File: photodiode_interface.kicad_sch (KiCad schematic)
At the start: 41 parts, among them J4 Conn_01x12_Pin, J5 Conn_01x12_Pin, J6 Conn_01x12_Pin, J7 Conn_01x12_Pin, U5 OPA350, U6 SN74LVC16244ADGGR, U7 SN74LVC32A

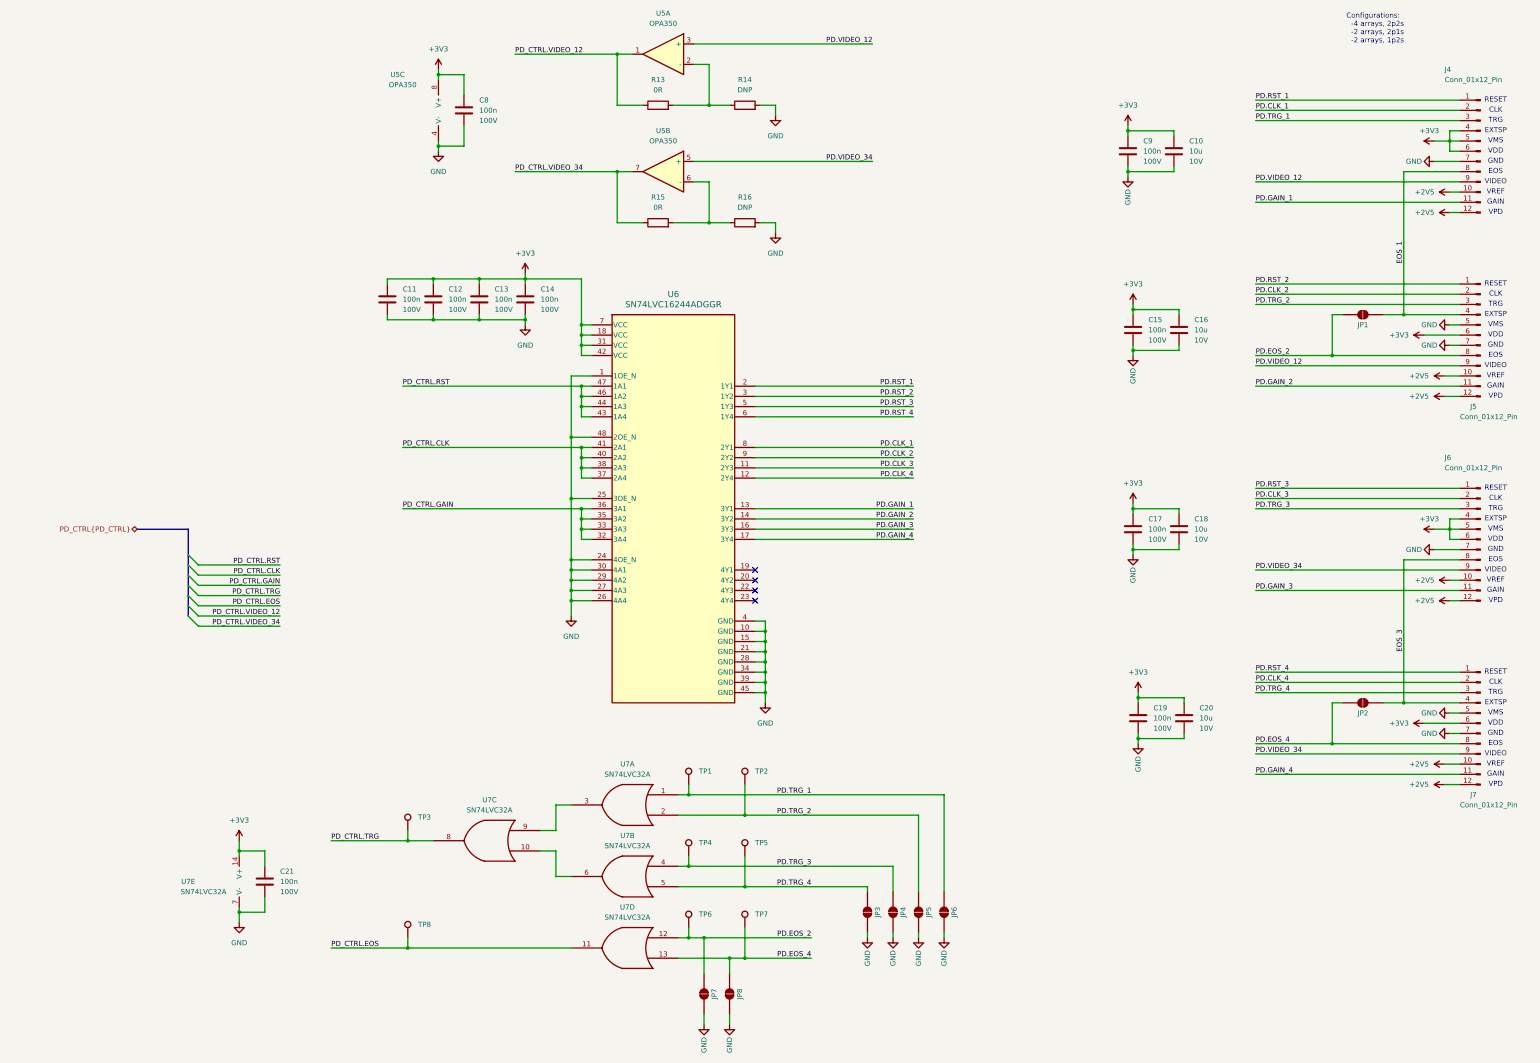
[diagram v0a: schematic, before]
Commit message: nodified according to review
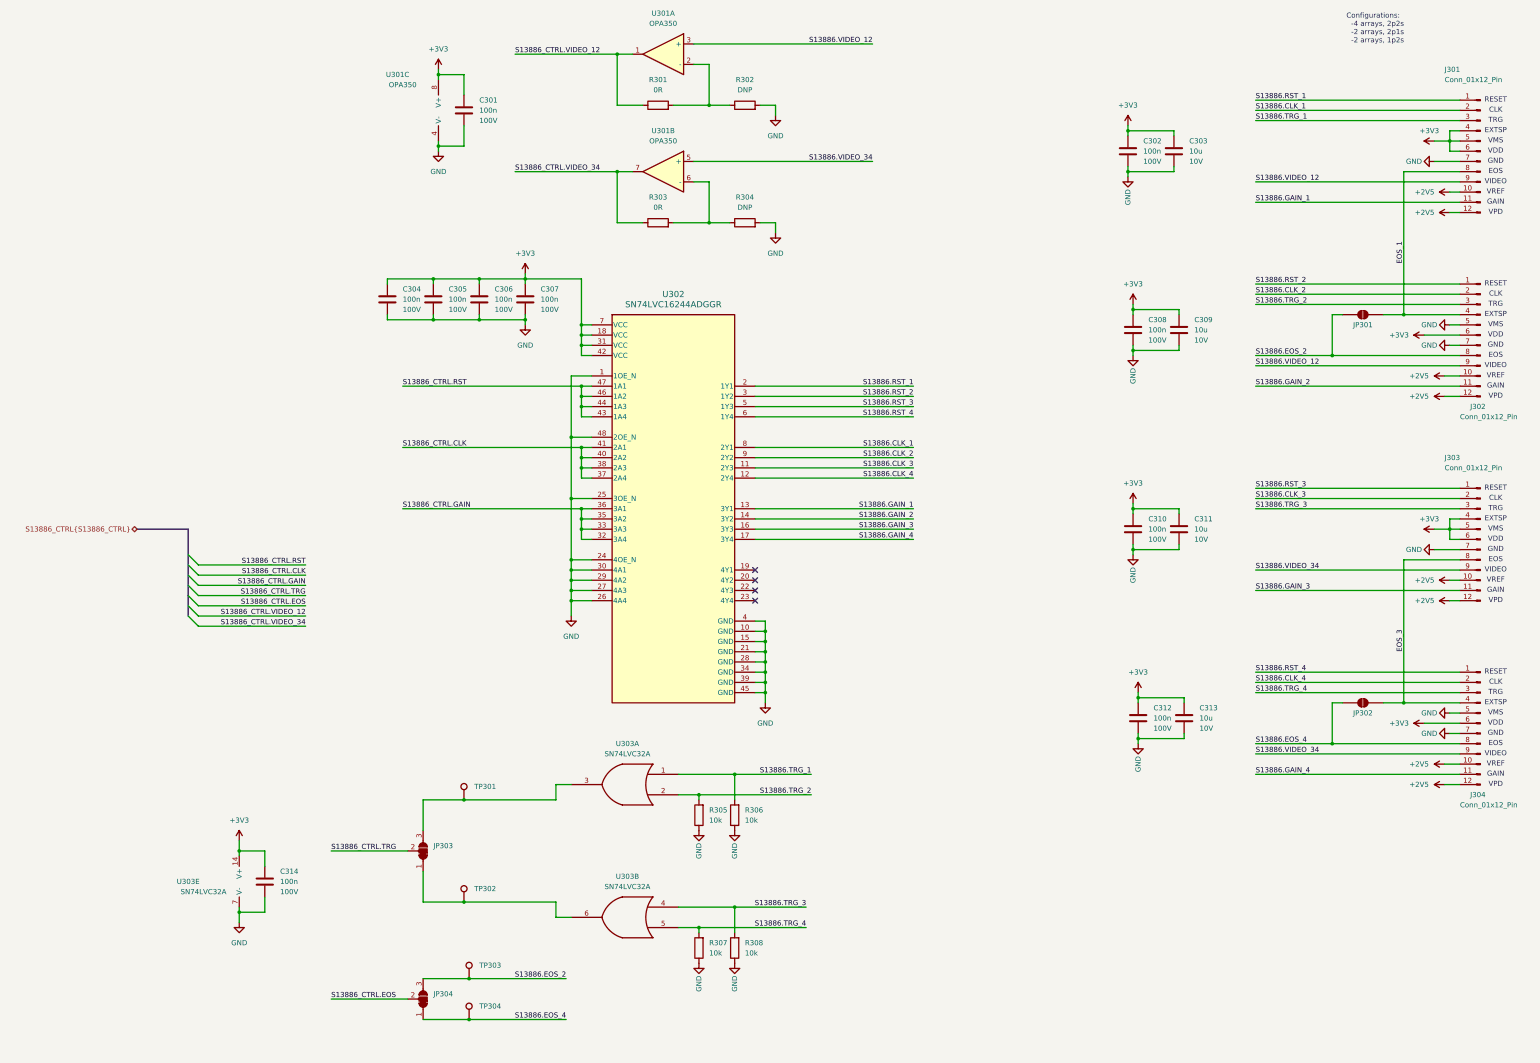
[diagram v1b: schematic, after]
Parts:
- removed JP3, JP4, JP5, JP6, JP7, JP8: SolderJumper_2_Open, symbol Jumper:SolderJumper_2_Open
- removed TP1, TP2, TP3, TP4, TP5, TP8: TestPoint, symbol Connector:TestPoint
- removed unit 4 of U7
- removed unit 3 of U7
- added JP303, JP304: SolderJumper_3_Bridged12, symbol Jumper:SolderJumper_3_Bridged12
- added R305, R306, R307, R308: 10k, symbol Device:R
- added TP301, TP302: TestPoint, symbol Connector:TestPoint
- renumbered C8 to C301, C9 to C302, C10 to C303, C11 to C304, C12 to C305, C13 to C306, C14 to C307, C15 to C308, C16 to C309, C17 to C310, C18 to C311, C19 to C312, C20 to C313, C21 to C314, J4 to J301, J5 to J302, J6 to J303, J7 to J304, JP1 to JP301, JP2 to JP302, R13 to R301, R14 to R302, R15 to R303, R16 to R304, TP6 to TP303, TP7 to TP304, U5 to U301, U6 to U302, U7 to U303
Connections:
- net GND: now also R305.1, R306.1, R307.1, R308.1
- net at U303.3: now also JP303.3 (B), TP301.1
- net at U303.6: now also JP303.1 (A), TP302.1
- net PD.CLK_1 renamed S13886.CLK_1
- net PD.CLK_2 renamed S13886.CLK_2
- net PD.CLK_3 renamed S13886.CLK_3
- net PD.CLK_4 renamed S13886.CLK_4
- net PD.EOS_2 renamed S13886.EOS_2
- net S13886.EOS_2: now also JP304.3 (B)
- net PD.EOS_4 renamed S13886.EOS_4
- net S13886.EOS_4: now also JP304.1 (A)
- net PD.GAIN_1 renamed S13886.GAIN_1
- net PD.GAIN_2 renamed S13886.GAIN_2
- net PD.GAIN_3 renamed S13886.GAIN_3
- net PD.GAIN_4 renamed S13886.GAIN_4
- net PD.RST_1 renamed S13886.RST_1
- net PD.RST_2 renamed S13886.RST_2
- net PD.RST_3 renamed S13886.RST_3
- net PD.RST_4 renamed S13886.RST_4
- net PD.TRG_1 renamed S13886.TRG_1
- net S13886.TRG_1: now also R306.2
- net PD.TRG_2 renamed S13886.TRG_2
- net S13886.TRG_2: now also R305.2
- net PD.TRG_3 renamed S13886.TRG_3
- net S13886.TRG_3: now also R308.2
- net PD.TRG_4 renamed S13886.TRG_4
- net S13886.TRG_4: now also R307.2
- net PD.VIDEO_12 renamed S13886.VIDEO_12
- net PD.VIDEO_34 renamed S13886.VIDEO_34
- net PD_CTRL.CLK renamed S13886_CTRL.CLK
- net PD_CTRL.GAIN renamed S13886_CTRL.GAIN
- net PD_CTRL.RST renamed S13886_CTRL.RST
- net PD_CTRL.VIDEO_12 renamed S13886_CTRL.VIDEO_12
- net PD_CTRL.VIDEO_34 renamed S13886_CTRL.VIDEO_34
- new net S13886_CTRL.EOS: JP304.2 (C)
- new net S13886_CTRL.TRG: JP303.2 (C)
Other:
- company: (none) -> Protonica
- title: (none) -> Front End Electronics
- moved on the sheet: TP303, TP304, U303A, U303B

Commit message: minor changes
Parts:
- removed JP303, JP304: SolderJumper_3_Bridged12, symbol Jumper:SolderJumper_3_Bridged12
- added JP303, JP305: SolderJumper_3_Open, symbol Jumper:SolderJumper_3_Open
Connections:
- net S13886.EOS_2: now also JP303.3 (B)
- net S13886.EOS_4: now also JP303.1 (A)
- net S13886_CTRL.EOS: now also JP303.2 (C)
- net S13886_CTRL.TRG: now also JP305.2 (C)
- net at TP301.1, U303.3: now also JP305.3 (B)
- net at TP302.1, U303.6: now also JP305.1 (A)
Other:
- note added: "Configurations: -4 arrays, 2p2s => JP301 OFF, JP302 OFF -2 arrays, 2p1s => PD1 and PD3, JP301 ON, JP302 ON -2 arrays, 1p2s => PD1 and PD2, JP301 OFF, JP302 OFF"
- note removed: "Configurations: -4 arrays, 2p2s -2 arrays, 2p1s -2 arrays, 1p2s"

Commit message: footprints associated to symbols
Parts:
- C301, C302, C304, C305, C306, C307, C308, C310, C312, C314: footprint (none) -> Capacitor_SMD:C_0805_2012Metric_Pad1.18x1.45mm_HandSolder; MPN (none) -> GCM21BR72A104KA37L; Manufacturer (none) -> Murata Electronics
- C303, C309, C311, C313: footprint (none) -> Capacitor_SMD:C_1206_3216Metric_Pad1.33x1.80mm_HandSolder; MPN (none) -> GRM31CR71E106KA12L; Manufacturer (none) -> Murata Electronics; Voltage 10V -> 25V
- J301, J302, J303, J304: footprint (none) -> Connector_PinHeader_2.54mm:PinHeader_1x12_P2.54mm_Vertical
- JP301, JP302: footprint (none) -> Jumper:SolderJumper-2_P1.3mm_Open_Pad1.0x1.5mm
- JP303, JP305: footprint (none) -> Jumper:SolderJumper-3_P1.3mm_Open_Pad1.0x1.5mm
- R301, R303: footprint (none) -> Resistor_SMD:R_0805_2012Metric_Pad1.20x1.40mm_HandSolder; MPN (none) -> CRCW08050000Z0EA; Manufacturer (none) -> Vishay Dale
- R302, R304: footprint (none) -> Resistor_SMD:R_0805_2012Metric_Pad1.20x1.40mm_HandSolder
- R305, R306, R307, R308: footprint (none) -> Resistor_SMD:R_0805_2012Metric_Pad1.20x1.40mm_HandSolder; MPN (none) -> CRCW080510K0FKEA; Manufacturer (none) -> Vishay Dale
- TP301, TP302, TP303, TP304: footprint (none) -> TestPoint:TestPoint_Keystone_5005-5009_Compact; MPN (none) -> 5005; Manufacturer (none) -> Keystone Electronics
- U301: footprint (none) -> Package_SO:SOIC-8_3.9x4.9mm_P1.27mm; MPN (none) -> OPA350UA/2K5; Manufacturer (none) -> Texas Instruments
- U302: footprint (none) -> Package_SO:TSSOP-48_6.1x12.5mm_P0.5mm; MPN (none) -> SN74LVC16244ADGGR; Manufacturer (none) -> Texas Instrument
- U303: footprint (none) -> Package_SO:SOIC-14_3.9x8.7mm_P1.27mm; MPN (none) -> SN74LVC32ADR; Manufacturer (none) -> Texas Instrument

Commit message: Most tracks routed
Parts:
- removed U303: SN74LVC32A, Package_SO:SOIC-14_3.9x8.7mm_P1.27mm, symbol Logic_Gates_Protonica:SN74LVC32A
- added U303: 74LVC2G32, Package_SO:VSSOP-8_3x3mm_P0.65mm, symbol 74xGxx:74LVC2G32
- J301, J302, J303, J304: footprint Connector_PinHeader_2.54mm:PinHeader_1x12_P2.54mm_Vertical -> Connector_PinHeader_2.54mm:PinHeader_2x06_P2.54mm_Vertical
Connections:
- net +3V3: now also U303.8 (VCC)
- net GND: now also U303.4 (GND)
- net S13886.TRG_1: now also U303.1
- net S13886.TRG_2: now also U303.2
- net S13886.TRG_3: now also U303.5
- net S13886.TRG_4: now also U303.6
- net at JP305.3 (B), TP301.1: now also U303.7
- net at JP305.1 (A), TP302.1: now also U303.3

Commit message: DRC clean
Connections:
- net TRG_12: now reaches JP305.3 (B), TP301.1, U303.7
- net TRG_34: now reaches JP305.1 (A), TP302.1, U303.3
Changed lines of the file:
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@@
+		)
+	)
+	(label "TRG_34"
+		(at 139.7 243.84 0)
+		(effects
+			(font
+				(size 1.27 1.27)
+			)
+			(justify left bottom)
 		)
 	)
@@
 		(effects
 			(font
+				(size 1.27 1.27)
+			)
+			(justify left bottom)
+		)
+	)
+	(label "TRG_12"
+		(at 139.7 218.44 0)
+		(effects
+			(font

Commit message: added stitching vias and silkscreen
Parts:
- added FB301: 220R@100MHz, Inductor_SMD:L_0805_2012Metric_Pad1.05x1.20mm_HandSolder, symbol Device:FerriteBead
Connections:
- net +3V3: now also FB301.1; no longer C301.1, U301.8 (V+)
- new net: C301.1, FB301.2, U301.8 (V+)
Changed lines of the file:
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@@
 	(title_block
 		(title "Front End Electronics")
-		(date "2026-05-05")
+		(date "2026-06-11")
 		(rev "B.1")
 		(company "Protonica")
@@
 	)
 	(junction
+		(at 120.65 38.1)
+		(diameter 0)
+		(color 0 0 0 0)
+	)
+	(junction
 		(at 292.1 52.07)
 		(diameter 0)
@@
 	)
 	(junction
-		(at 120.65 38.1)
-		(diameter 0)
-		(color 0 0 0 0)
-	)
-	(junction
 		(at 119.38 99.06)
 		(diameter 0)
@@
 	(wire
 		(pts
+			(xy 101.6 38.1) (xy 109.22 38.1)
+		)
+		(stroke
+			(width 0)
+			(type default)
+		)
+	)
+	(wire
+		(pts
 			(xy 201.93 184.15) (xy 201.93 186.69)
 		)
@@
 	(wire
 		(pts
-			(xy 120.65 36.83) (xy 120.65 38.1)
+			(xy 130.81 88.9) (xy 130.81 90.17)
 		)
 		(stroke
@@
 	(wire
 		(pts
-			(xy 130.81 88.9) (xy 130.81 90.17)
+			(xy 368.3 156.21) (xy 374.65 156.21)
 		)
 		(stroke
@@
 	(wire
 		(pts
-			(xy 368.3 156.21) (xy 374.65 156.21)
+			(xy 323.85 64.77) (xy 374.65 64.77)
 		)
 		(stroke
@@
 	(wire
 		(pts
-			(xy 323.85 64.77) (xy 374.65 64.77)
+			(xy 199.39 179.07) (xy 201.93 179.07)
 		)
 		(stroke
@@
 	(wire
 		(pts
-			(xy 199.39 179.07) (xy 201.93 179.07)
+			(xy 153.67 128.27) (xy 153.67 113.03)
 		)
 		(stroke
@@
 	(wire
 		(pts
-			(xy 153.67 128.27) (xy 153.67 113.03)
+			(xy 116.84 38.1) (xy 120.65 38.1)
 		)
 		(stroke
@@
 	(wire
 		(pts
+			(xy 101.6 36.83) (xy 101.6 38.1)
+		)
+		(stroke
+			(width 0)
+			(type default)
+		)
+	)
+	(wire
+		(pts
 			(xy 323.85 107.95) (xy 342.9 107.95)
 		)
@@
 	(symbol
 		(lib_id "power:+2V5")
-		(at 120.65 36.83 0)
+		(at 101.6 36.83 0)
 		(unit 1)
 		(body_style 1)
@@
 		(fields_autoplaced yes)
 		(property "Reference" "#PWR0301"
-			(at 120.65 40.64 0)
+			(at 101.6 40.64 0)
 			(hide yes)
 			(show_name no)
@@
 		)
 		(property "Value" "+3V3"
-			(at 120.65 31.75 0)
+			(at 101.6 31.75 0)
 			(show_name no)
 			(do_not_autoplace no)
@@
 		)
 		(property "Footprint" ""
-			(at 120.65 36.83 0)
+			(at 101.6 36.83 0)
 			(hide yes)
 			(show_name no)
@@
 		)
 		(property "Datasheet" ""
-			(at 120.65 36.83 0)
+			(at 101.6 36.83 0)
 			(hide yes)
 			(show_name no)
@@
 		)
 		(property "Description" "Power symbol creates a global label with name \"+2V5\""
-			(at 120.65 36.83 0)
+			(at 101.6 36.83 0)
 			(hide yes)
 			(show_name no)
@@
 	)
 	(symbol
+		(lib_id "Device:FerriteBead")
+		(at 113.03 38.1 90)
+		(unit 1)
+		(body_style 1)
+		(exclude_from_sim no)
+		(in_bom yes)
+		(on_board yes)
+		(in_pos_files yes)
+		(dnp no)
+		(fields_autoplaced yes)
+		(property "Reference" "FB301"
+			(at 112.9792 30.48 90)
+			(show_name no)
+			(do_not_autoplace no)
+			(effects
+				(font
+					(size 1.27 1.27)
+				)
+			)
+		)
+		(property "Value" "220R@100MHz"
+			(at 112.9792 33.02 90)
+			(show_name no)
+			(do_not_autoplace no)
+			(effects
+				(font
+					(size 1.27 1.27)
+				)
+			)
+		)
+		(property "Footprint" "Inductor_SMD:L_0805_2012Metric_Pad1.05x1.20mm_HandSolder"
+			(at 113.03 39.878 90)
+			(hide yes)
+			(show_name no)
+			(do_not_autoplace no)
+			(effects
+				(font
+					(size 1.27 1.27)
+				)
+			)
+		)
+		(property "Datasheet" ""
+			(at 113.03 38.1 0)
+			(hide yes)
+			(show_name no)
+			(do_not_autoplace no)
+			(effects
+				(font
+					(size 1.27 1.27)
+				)
+			)
+		)
+		(property "Description" "FERRITE BEAD 220 OHM 0805 1LN"
+			(at 113.03 38.1 0)
+			(hide yes)
+			(show_name no)
+			(do_not_autoplace no)
+			(effects
+				(font
+					(size 1.27 1.27)
+				)
+			)
+		)
+		(property "MPN" "BLM21PG221SN1D"
+			(at 113.03 38.1 90)
+			(hide yes)
+			(show_name no)
+			(do_not_autoplace no)
+			(effects
+				(font
+					(size 1.27 1.27)
+				)
+			)
+		)
+		(property "Manufacturer" "Murata Electronics"
+			(at 113.03 38.1 90)
+			(hide yes)
+			(show_name no)
+			(do_not_autoplace no)
+			(effects
+				(font
+					(size 1.27 1.27)
+				)
+			)
+		)
+		(property "L (µH)" ""
+			(at 113.03 38.1 90)
+			(hide yes)
+			(show_name no)
+			(do_not_autoplace no)
+			(effects
+				(font
+					(size 1.27 1.27)
+				)
+			)
+		)
+		(pin "1"
+		)
+		(pin "2"
+		)
+		(instances
+			(project "hw-front-end"
+				(path "/87f042ce-f629-4310-aed7-dea93cc7b6f7/4abb1a1f-8324-42a5-a74a-0cb17502f086"
+					(reference "FB301")
+					(unit 1)
+				)
+			)
+		)
+	)
+	(symbol
 		(lib_id "power:GND")
 		(at 372.11 100.33 270)
@@
 		(in_pos_files yes)
 		(dnp no)
+		(fields_autoplaced yes)
 		(property "Reference" "U301"
-			(at 110.49 38.1 0)
+			(at 119.38 45.7199 0)
 			(show_name no)
 			(do_not_autoplace no)
@@
 					(size 1.27 1.27)
 				)
+				(justify left)
 			)
 		)
 		(property "Value" "OPA350"
-			(at 111.76 40.64 0)
+			(at 119.38 48.2599 0)
 			(show_name no)
 			(do_not_autoplace no)
@@
 					(size 1.27 1.27)
 				)
+				(justify left)
 			)
 		)

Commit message: minor changes
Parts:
- J301, J302, J303, J304: value Conn_01x12_Pin -> Conn_02x06_Pin; MPN (none) -> G800W590018EU; Manufacturer (none) -> Amphenol ICC
- U301: MPN OPA350UA/2K5 -> OPA350UA/2K5
- U302, U303: Manufacturer Texas Instrument -> Texas Instruments
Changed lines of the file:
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@@
 			)
 		)
-		(property "Value" "Conn_01x12_Pin"
+		(property "Value" "Conn_02x06_Pin"
 			(at 370.84 39.37 0)
 			(show_name no)
@@
 			)
 		)
-		(property "Description" "CONN HEADER R/A 12POS 2.54MM"
+		(property "Description" "CONN HEADER VERTICAL 12POS 2.54MM"
 			(at 379.73 57.15 0)
 			(hide yes)
@@
 			)
 		)
-		(property "MPN" ""
+		(property "MPN" "G800W590018EU"
 			(at 379.73 57.15 0)
 			(hide yes)
@@
 			)
 		)
-		(property "Manufacturer" ""
+		(property "Manufacturer" "Amphenol ICC"
 			(at 379.73 57.15 0)
 			(hide yes)
@@
 			)
 		)
-		(property "MPN" " OPA350UA/2K5"
+		(property "MPN" "OPA350UA/2K5"
 			(at 176.53 62.23 0)
 			(hide yes)
@@
 			)
 		)
-		(property "Value" "Conn_01x12_Pin"
+		(property "Value" "Conn_02x06_Pin"
 			(at 374.65 123.19 0)
 			(show_name no)
@@
 			)
 		)
-		(property "Description" "CONN HEADER R/A 12POS 2.54MM"
+		(property "Description" "CONN HEADER VERTICAL 12POS 2.54MM"
 			(at 379.73 102.87 0)
 			(hide yes)
@@
 			)
 		)
-		(property "MPN" ""
+		(property "MPN" "G800W590018EU"
 			(at 379.73 102.87 0)
 			(hide yes)
@@
 			)
 		)
-		(property "Manufacturer" ""
+		(property "Manufacturer" "Amphenol ICC"
 			(at 379.73 102.87 0)
 			(hide yes)
@@
 			)
 		)
-		(property "Manufacturer" "Texas Instrument"
+		(property "Manufacturer" "Texas Instruments"
 			(at 165.1 247.65 0)
 			(hide yes)
@@
 			)
 		)
-		(property "Manufacturer" "Texas Instrument"
+		(property "Manufacturer" "Texas Instruments"
 			(at 67.31 238.76 0)
 			(hide yes)
@@
 			)
 		)
-		(property "Value" "Conn_01x12_Pin"
+		(property "Value" "Conn_02x06_Pin"
 			(at 370.84 135.89 0)
 			(show_name no)
@@
 			)
 		)
-		(property "Description" "CONN HEADER R/A 12POS 2.54MM"
+		(property "Description" "CONN HEADER VERTICAL 12POS 2.54MM"
 			(at 379.73 153.67 0)
 			(hide yes)
@@
 			)
 		)
-		(property "MPN" ""
+		(property "MPN" "G800W590018EU"
 			(at 379.73 153.67 0)
 			(hide yes)
@@
 			)
 		)
-		(property "Manufacturer" ""
+		(property "Manufacturer" "Amphenol ICC"
 			(at 379.73 153.67 0)
 			(hide yes)
@@
 			)
 		)
-		(property "Value" "Conn_01x12_Pin"
+		(property "Value" "Conn_02x06_Pin"
 			(at 374.65 219.71 0)
 			(show_name no)
@@
 			)
 		)
-		(property "Description" "CONN HEADER R/A 12POS 2.54MM"
+		(property "Description" "CONN HEADER VERTICAL 12POS 2.54MM"
 			(at 379.73 199.39 0)
 			(hide yes)
@@
 			)
 		)
-		(property "MPN" ""
+		(property "MPN" "G800W590018EU"
 			(at 379.73 199.39 0)
 			(hide yes)
@@
 			)
 		)
-		(property "Manufacturer" ""
+		(property "Manufacturer" "Amphenol ICC"
 			(at 379.73 199.39 0)
 			(hide yes)
@@
 			)
 		)
-		(property "MPN" " OPA350UA/2K5"
+		(property "MPN" "OPA350UA/2K5"
 			(at 176.53 33.02 0)
 			(hide yes)
@@
 			)
 		)
-		(property "Manufacturer" "Texas Instrument"
+		(property "Manufacturer" "Texas Instruments"
 			(at 165.1 214.63 0)
 			(hide yes)
@@
 			)
 		)
-		(property "Manufacturer" "Texas Instrument"
+		(property "Manufacturer" "Texas Instruments"
 			(at 158.75 100.33 0)
 			(hide yes)
@@
 			)
 		)
-		(property "MPN" " OPA350UA/2K5"
+		(property "MPN" "OPA350UA/2K5"
 			(at 118.11 46.99 0)
 			(hide yes)
